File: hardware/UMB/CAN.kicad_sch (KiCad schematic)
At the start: 15 parts, among them U15 ADM3057ExRW

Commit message: Power section done
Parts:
- C10: renamed from C12; Mouser (none) -> https://www.mouser.pl/ProductDetail/Murata-Electronics/GRM2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; Mouser No (none) -> 81-GRM21BR61A476ME5L
- C11: renamed from C9; Mouser (none) -> https://www.mouser.pl/ProductDetail/KEMET/C0603C104M4RACAUT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; Mouser No (none) -> 80-C0603C104M4RAUTO
- C12: renamed from C10; Mouser (none) -> https://www.mouser.pl/ProductDetail/KEMET/C0603C103J5RACAUT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; Mouser No (none) -> 80-C0603C103J5RAUTO
- C13: renamed from C72; Mouser (none) -> https://www.mouser.pl/ProductDetail/Walsin/S252B222K502CT?q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; Mouser No (none) -> 791-S252B222K502CT
- C5, C7: Mouser (none) -> https://www.mouser.pl/ProductDetail/Murata-Electronics/GRM2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; Mouser No (none) -> 81-GRM21BR61A476ME5L
- C6: Mouser (none) -> https://www.mouser.pl/ProductDetail/KEMET/C0603C104M4RACAUT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; Mouser No (none) -> 80-C0603C104M4RAUTO
- C8: Mouser (none) -> https://www.mouser.pl/ProductDetail/KEMET/C0603C103J5RACAUT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; Mouser No (none) -> 80-C0603C103J5RAUTO
- C9: renamed from C11; Mouser (none) -> https://www.mouser.pl/ProductDetail/Murata-Electronics/GRM2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; Mouser No (none) -> 81-GRM21BR61A476ME5L
- R8: value 100K -> 100k
- renumbered FB2 to FB1, FB5 to FB2, U15 to U3

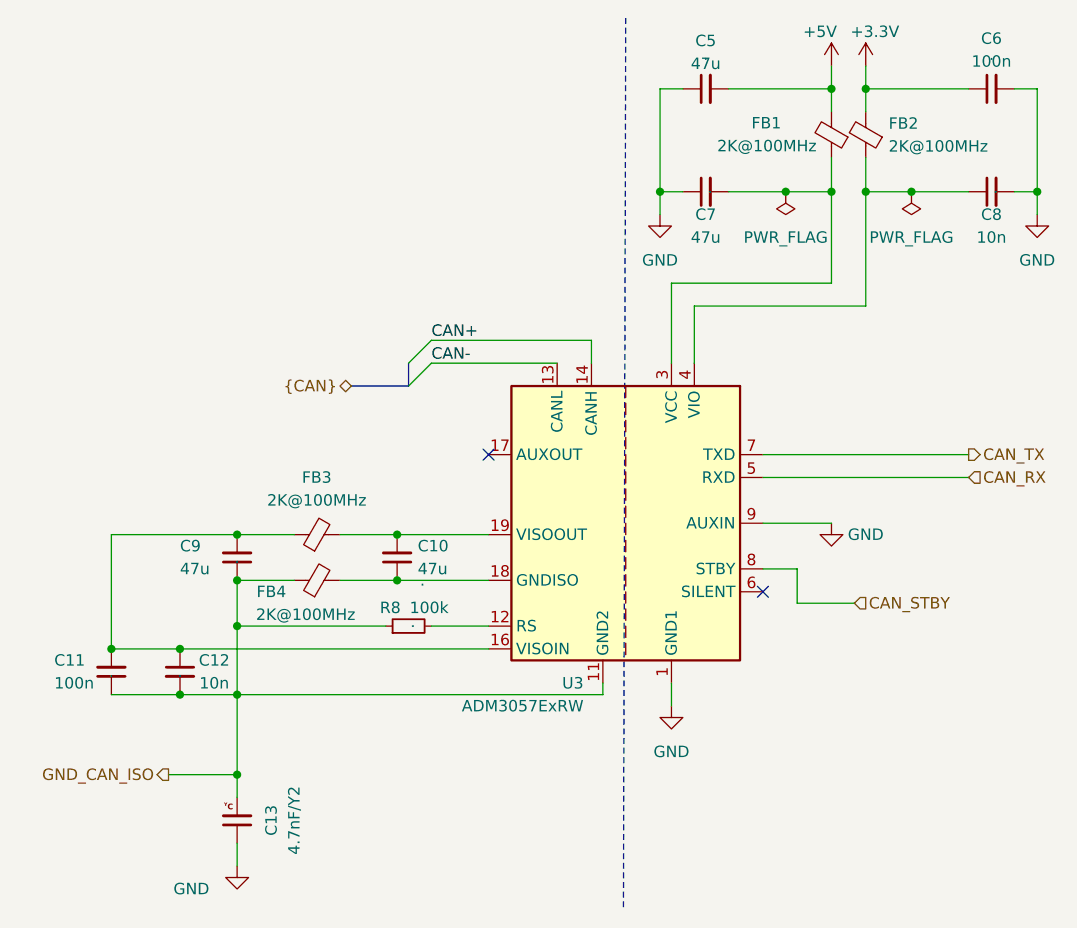
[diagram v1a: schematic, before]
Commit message: Added all footprints and parts Mouser IDs
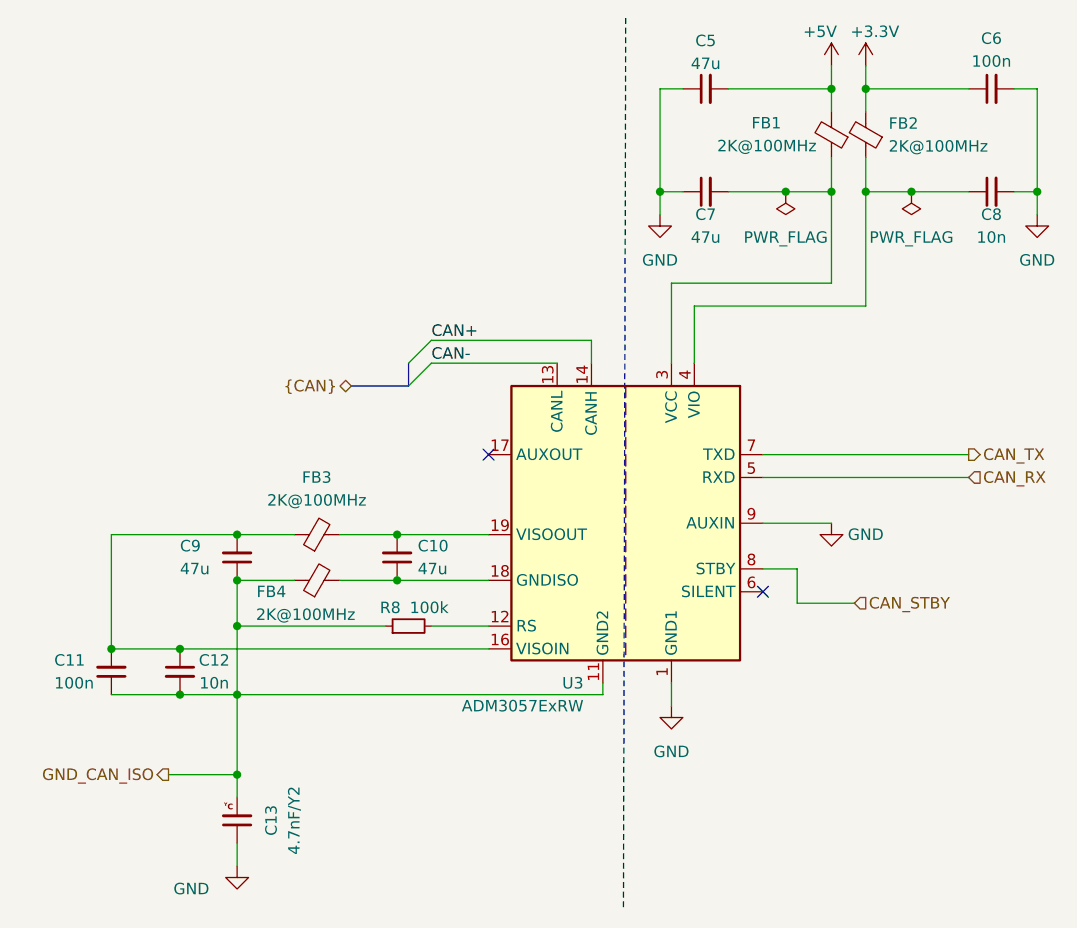
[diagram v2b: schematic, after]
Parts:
- C10, C5, C7, C9: Manufacturer_Part_Number (none) -> GRM21BR61A476ME15L; Mouser Part Number . -> (none)
- C11, C6: Manufacturer_Part_Number (none) -> C0603C104M4RACAUTO; Mouser Part Number . -> (none)
- C12, C8: Manufacturer_Part_Number (none) -> C0603C103J5RACAUTO; Mouser Part Number . -> (none)
- C13: Height 2.8 -> (none); Manufacturer_Name Walsin Technology Corporation -> (none); Mouser Part Number 791-S252B222K502CT -> (none); Mouser Price/Stock https://www.mouser.co.uk/ProductDetail/Walsin/S252B222K502C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 -> (none)
- FB1, FB2, FB3, FB4: Manufacturer_Part_Number (none) -> 2508052027Y1; Mouser (none) -> https://www.mouser.pl/ProductDetail/Fair-Rite/2508052027Y1?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; Mouser No (none) -> 623-2508052027Y1; Mouser Part Number 623-2508052027Y1 -> (none)
- R8: Mouser (none) -> in warsztatowe zapasy i think; Mouser Part Number . -> (none)
- U3: Manufacturer_Part_Number (none) -> ADM3057EBRWZ; Mouser (none) -> https://www.mouser.pl/ProductDetail/Analog-Devices/ADM3057E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; Mouser No (none) -> 584-ADM3057EBRWZ; Mouser Part Number 584-ADM3057EBRWZ -> (none)
